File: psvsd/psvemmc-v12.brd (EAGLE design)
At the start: 41 x 22.5 mm, 36 parts, among them U1 USB2244QFN, U2 LP3996_DSC_10, U3 TXS02612, X1 ZX62D-B-5PA8, Y1 XRCGB

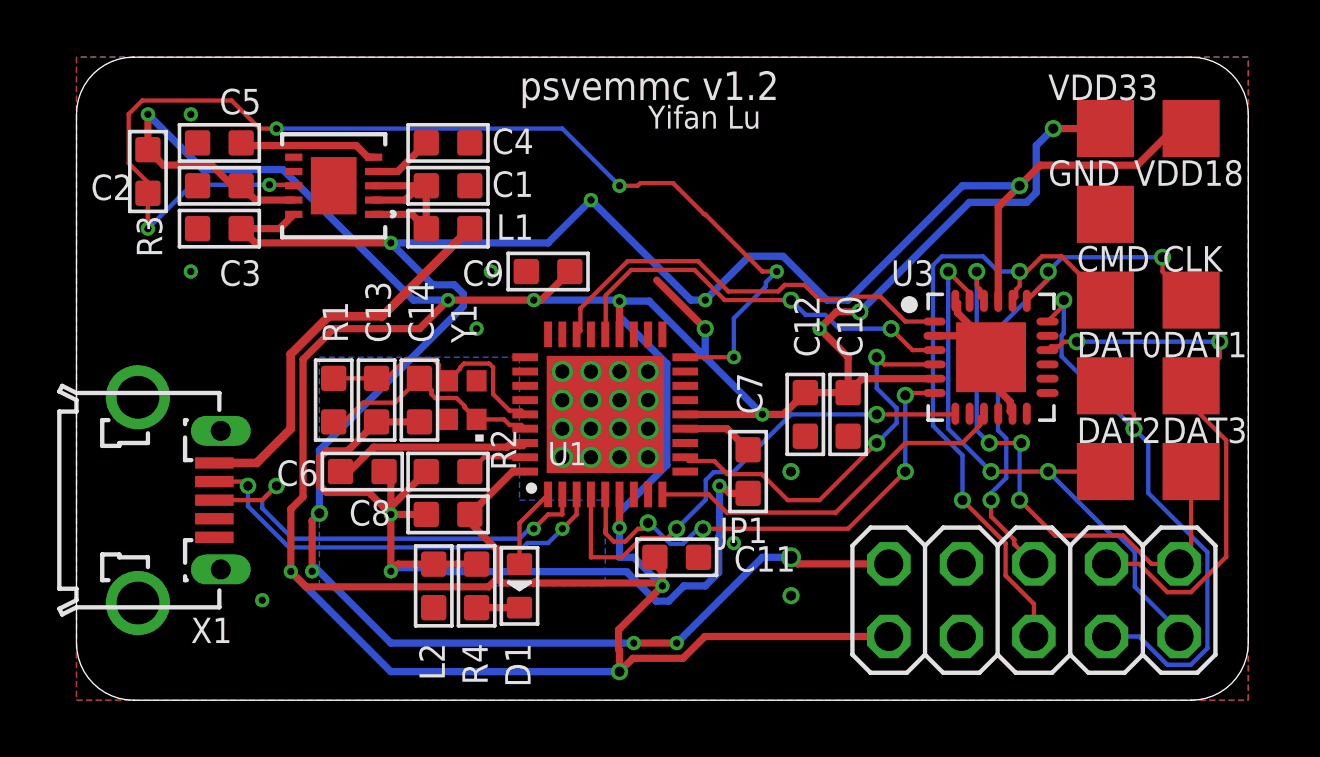
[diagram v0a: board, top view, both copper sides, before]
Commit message: psvemmc v1.2: unified drill sizes, added thermal vias to TTL translation IC
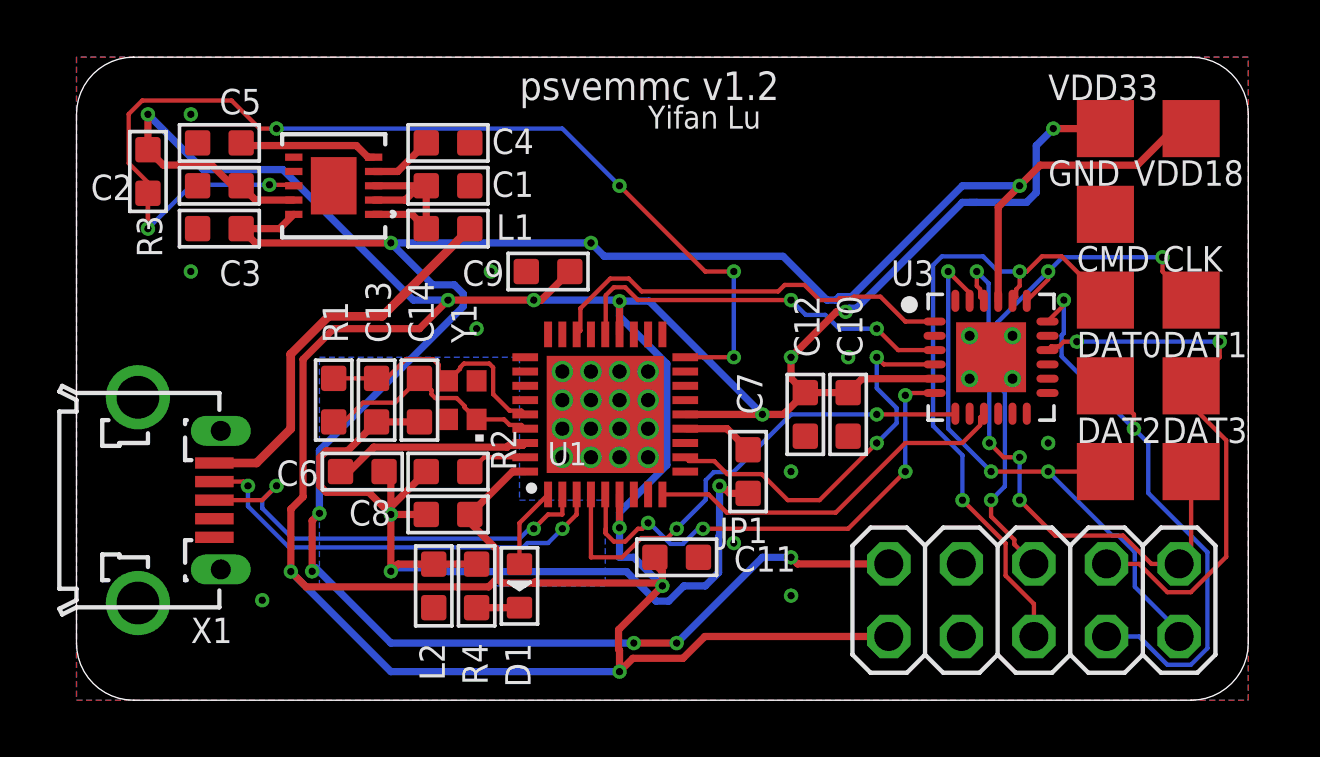
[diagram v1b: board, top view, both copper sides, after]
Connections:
- new net ECPAD: U3.EPAD
- net GND: no longer U3.EPAD
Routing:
- net GND: track 7.77 -> 3.71 mm, vias 24 -> 30
- net VDD33: track 138.5 -> 135.6 mm, vias 13 -> 12
- net VDD18: track 83.5 -> 81.0 mm, vias 9 -> 8
- net !RESET: track 42.0 -> 39.8 mm
- net SD_D2: track 15.4 -> 14.7 mm
- net SD_D3: track 14.4 -> 13.9 mm
